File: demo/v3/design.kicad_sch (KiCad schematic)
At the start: 9 parts, among them J1 5V_IN, J2 3V3_OUT, U1 3.3V

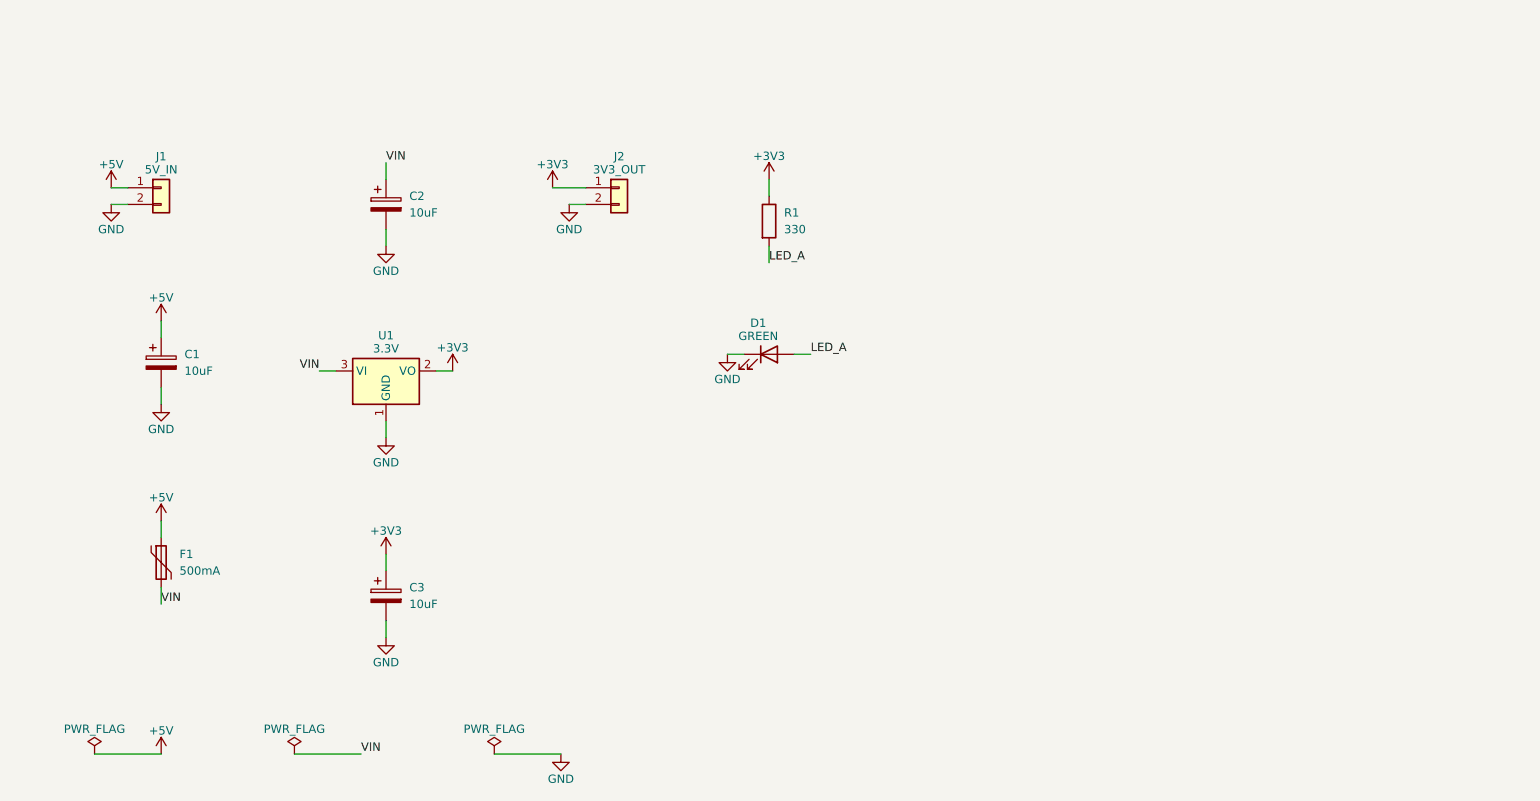
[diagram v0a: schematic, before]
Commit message: Draw schematics with routed wires; add MIC5317 and mounting-pin connector
Wired drafting is now the default: parts sit in a row on a common rail
line, a grid router draws each net as wires with junctions, each rail
gets one power symbol, and the sheet gets its title and a frame. A net
that cannot be routed falls back to the label style, which
hints.wiring "labels" also selects.

- lib/engine/wired.ts: row placement, connector mirroring, router,
  power-symbol and PWR_FLAG taps
- catalogue: Regulator_Linear:MIC5317-3.3xM5 and
  Connector_Generic_MountingPin:Conn_01x02_MountingPin; regulator
  rules accept VIN/VOUT pin names
- examples/mic5317-3v3.intent.json, with acceptance and engine tests
- studio: phone layout, 404 page, self-playing demo (?auto=1, ?start=N)
- demo and landing screenshot redrawn in the wired style
- eval re-run on the wired engine: 10/10 ERC-clean first time
- docs/LEARNINGS.md, docs/STACK.md, architecture diagram in README
- GitHub Actions workflow: type-check and build

Co-Authored-By: Claude Fable 5.1 <noreply@anthropic.com>
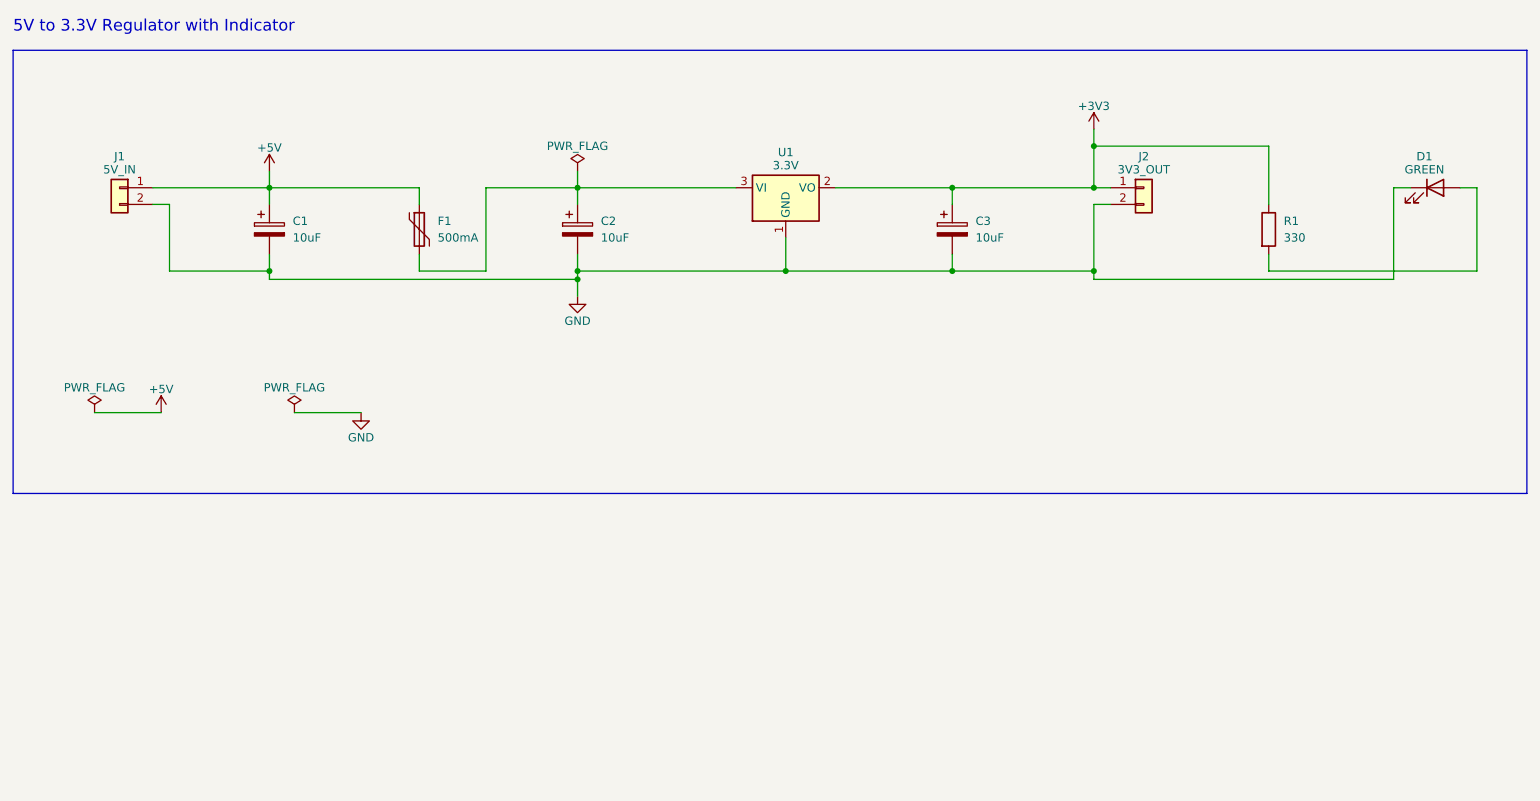
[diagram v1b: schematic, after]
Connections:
- net LED_A: no longer names the net of D1.2 (A), R1.2
- net VIN: no longer names the net of C2.1, F1.2, U1.3 (VI)
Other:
- note added: "5V to 3.3V Regulator with Indicator"
- moved on the sheet: C1, C2, C3, D1, F1, J1, J2, R1, U1

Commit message: Add the code-generated demo film pipeline and a new recorded demo
video/: script, edge-tts narration, HTML motion-graphics scenes in the
product's palette and fonts, Playwright rendering and product capture,
a generated music bed, and ffmpeg assembly. Rendered output and
intermediate files are git-ignored; video/README.md has the run order.

- demo/ now holds a five-step session recorded with live Gemma calls:
  draft, a question, a five-edit change, a deliberately broken version
  and its fix
- demo mode replays answers and the Keep bar as well as versions;
  ?film=1 types the messages and shortens the replay wait for recording
- every number in the film is read from the repo at render time

Co-Authored-By: Claude Fable 5.1 <noreply@anthropic.com>
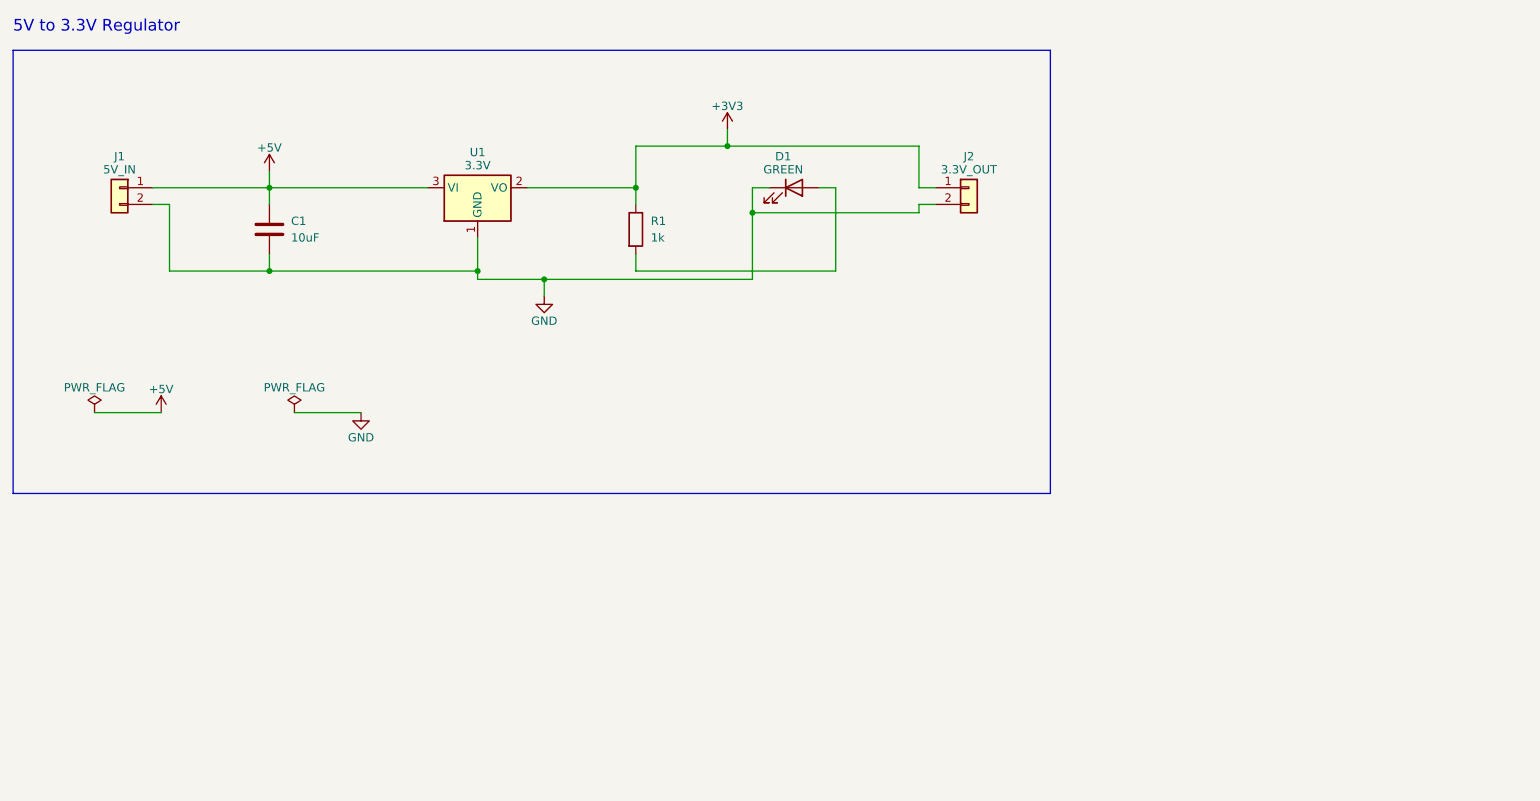
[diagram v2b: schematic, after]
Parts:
- removed C2, C3: 10uF, symbol Device:C_Polarized
- removed F1: 500mA, symbol Device:Polyfuse
- C1: symbol Device:C_Polarized -> Device:C
- J2: value 3V3_OUT -> 3.3V_OUT
- R1: value 330 -> 1k
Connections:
- net +5V: now also U1.3 (VI)
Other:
- note added: "5V to 3.3V Regulator"
- note removed: "5V to 3.3V Regulator with Indicator"
- title: 5V to 3.3V Regulator with Indicator -> 5V to 3.3V Regulator
- moved on the sheet: D1, J2, R1, U1
